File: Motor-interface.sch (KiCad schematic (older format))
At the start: 40 parts, among them K1 RELAY_2RT, P2 TE-23pins connector, Q1 Q_NPN_BCE, U2 Teensy_3.2

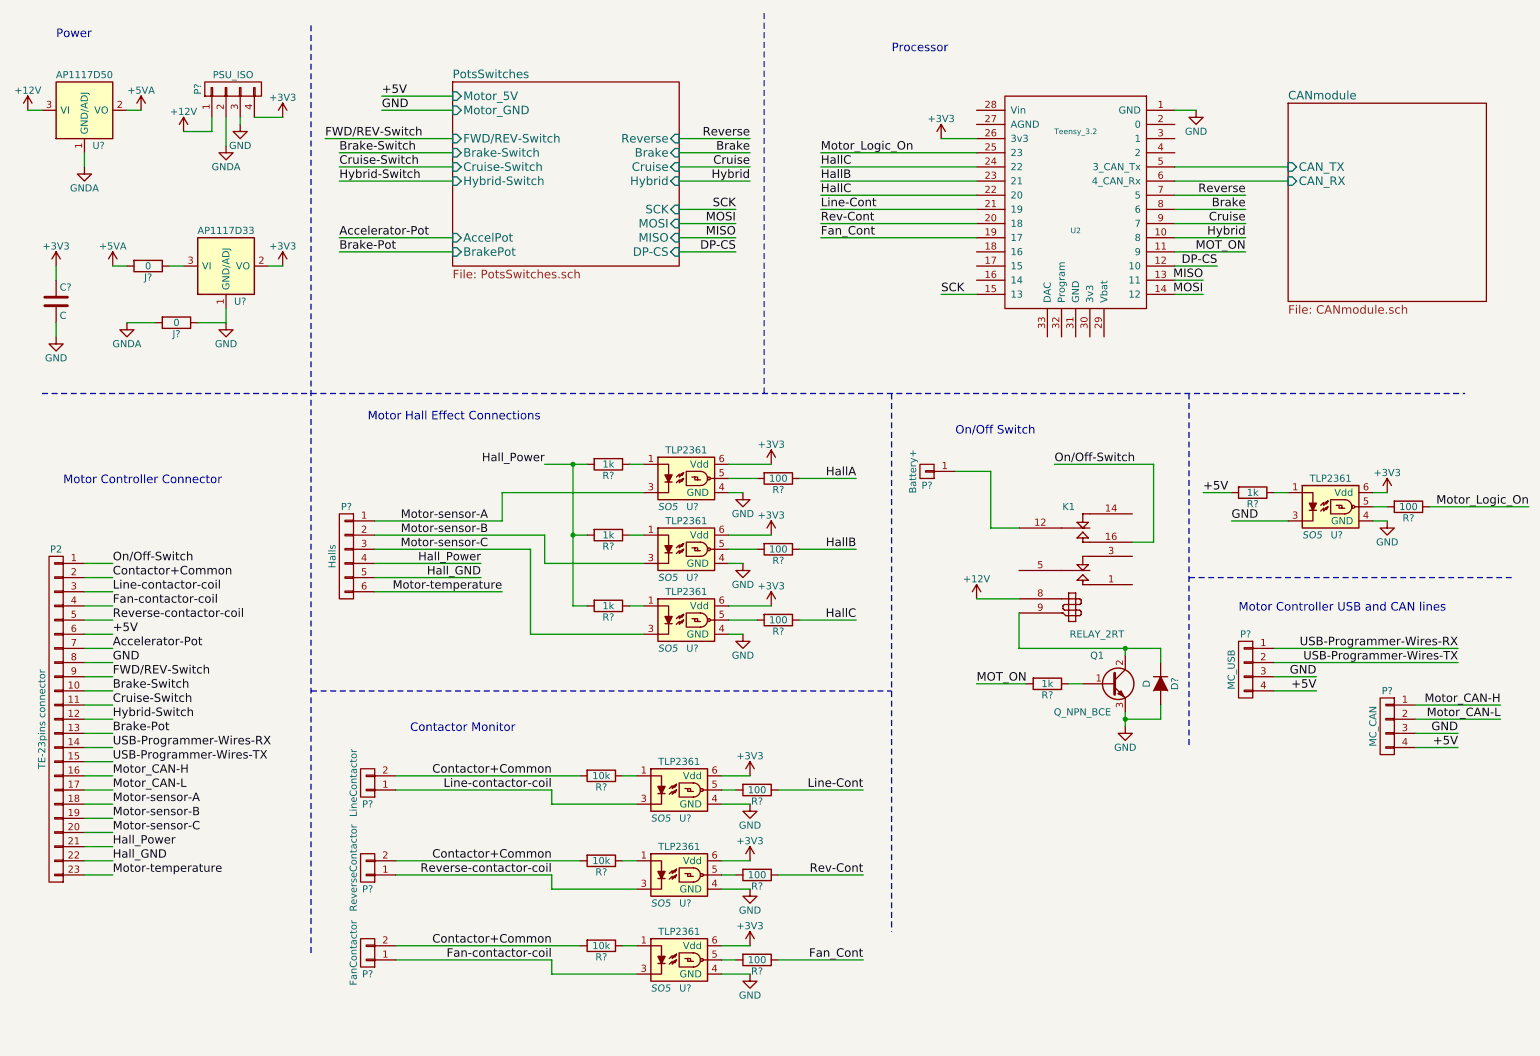
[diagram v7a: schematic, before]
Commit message: most associations, started pcb
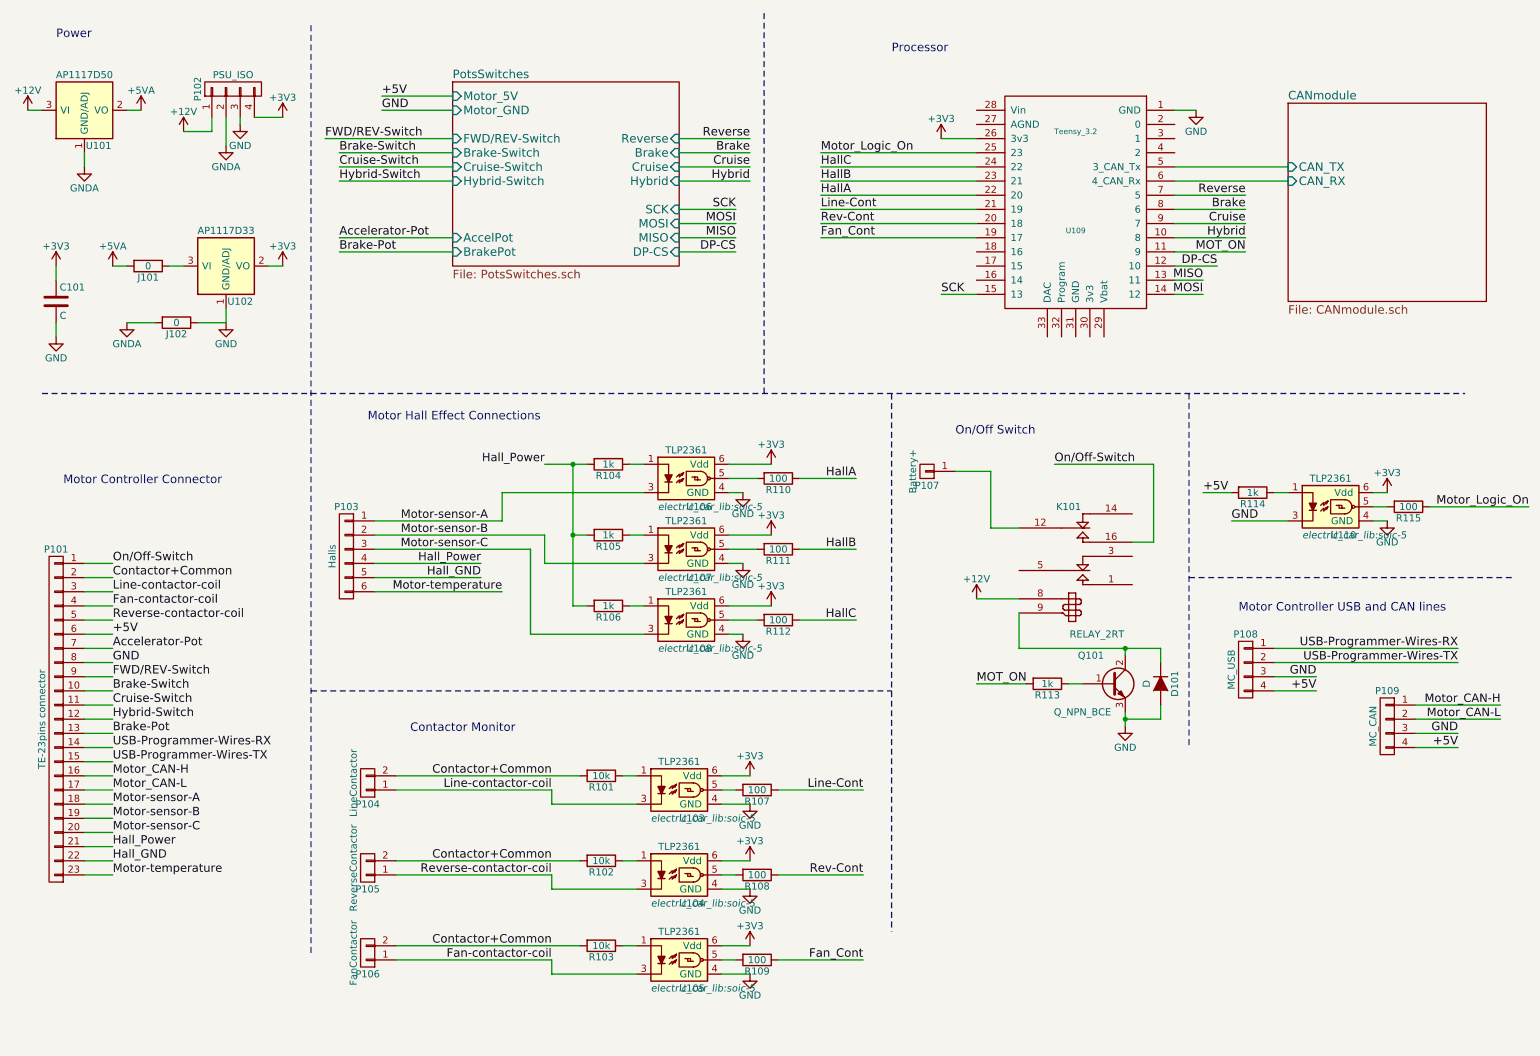
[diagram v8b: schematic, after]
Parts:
- C101: renamed from C?; footprint (none) -> Capacitors_SMD:C_1210_HandSoldering
- D101: renamed from D?; footprint (none) -> Diodes_SMD:DO-214AB_Handsoldering
- J101, J102: renamed from J?; footprint (none) -> Resistors_SMD:R_1210_HandSoldering
- P102, P108, P109: renamed from P?; footprint (none) -> Pin_Headers:Pin_Header_Straight_1x04
- P103: renamed from P?; footprint (none) -> Pin_Headers:Pin_Header_Straight_1x06
- P104, P105, P106: renamed from P?; footprint (none) -> Connect:bornier2
- R101, R102, R103, R104, R105, R106, R107, R108, R109, R110, R111, R112, R113, R114, R115: renamed from R?; footprint (none) -> Resistors_SMD:R_1206_HandSoldering
- U101, U102: renamed from U?; footprint (none) -> TO_SOT_Packages_SMD:TO-252-2Lead
- U103, U104, U105, U106, U107, U108, U110: renamed from U?; footprint SO5 -> electric_car_lib:soic-5
- gave numbers to parts that had none: 1
- renumbered K1 to K101, P2 to P101, Q1 to Q101, U2 to U109
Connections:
- net HallA: now also U109.22 (20)
- net HallC: no longer U109.22 (20)
